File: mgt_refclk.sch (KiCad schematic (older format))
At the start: 23 parts, among them U12 5P49V6965, Y1 25MHz

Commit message: WIP: point before we change to OSH/relaxed process
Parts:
- C83, C84: value C_Small -> 100n
- R64, R65: value 10k -> 3k3
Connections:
- net I2C_SCL renamed SCL_1
- net I2C_SDA renamed SDA_1
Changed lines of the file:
@@
 $Descr A4 11693 8268
 encoding utf-8
-Sheet 18 18
+Sheet 11 18
 Title ""
 Date ""
@@
 	4250 3300 4100 3300
 Text GLabel 4050 4000 0    50   BiDi ~ 0
-I2C_SCL
+SCL_1
 Text GLabel 4050 3900 0    50   BiDi ~ 0
-I2C_SDA
+SDA_1
 Wire Wire Line
 	4050 3900 4350 3900
@@
 AR Path="/61FA7DF7/61FB7439" Ref="R64"  Part="1"
 F 0 "R64" V 4450 3750 50  0000 C CNN
-F 1 "10k" V 4300 3750 50  0000 C CNN
+F 1 "3k3" V 4300 3750 50  0000 C CNN
 F 2 "Resistor_SMD:R_0603_1608Metric" H 4200 3750 50  0001 C CNN
 F 3 "~" H 4200 3750 50  0001 C CNN
@@
 AR Path="/61FA7DF7/61FB7508" Ref="R65"  Part="1"
 F 0 "R65" V 4550 3750 50  0000 C CNN
-F 1 "10k" V 4450 3750 50  0000 C CNN
+F 1 "3k3" V 4450 3750 50  0000 C CNN
 F 2 "Resistor_SMD:R_0603_1608Metric" H 4350 3750 50  0001 C CNN
 F 3 "~" H 4350 3750 50  0001 C CNN
@@
 P 7850 3750
 F 0 "C83" V 7621 3750 50  0000 C CNN
-F 1 "C_Small" V 7712 3750 50  0000 C CNN
+F 1 "100n" V 7712 3750 50  0000 C CNN
 F 2 "Capacitor_SMD:C_0603_1608Metric" H 7850 3750 50  0001 C CNN
 F 3 "~" H 7850 3750 50  0001 C CNN
@@
 P 7850 3950
 F 0 "C84" V 8050 3950 50  0000 C CNN
-F 1 "C_Small" V 7950 3950 50  0000 C CNN
+F 1 "100n" V 7950 3950 50  0000 C CNN
 F 2 "Capacitor_SMD:C_0603_1608Metric" H 7850 3950 50  0001 C CNN
 F 3 "~" H 7850 3950 50  0001 C CNN

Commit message: further work...
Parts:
- R66: value 1k78 -> 10k
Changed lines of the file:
@@
 $Descr A4 11693 8268
 encoding utf-8
-Sheet 11 18
+Sheet 11 20
 Title ""
 Date ""
@@
 AR Path="/61FA7DF7/61FC74BB" Ref="R66"  Part="1"
 F 0 "R66" V 5750 4600 50  0000 C CNN
-F 1 "1k78" V 5950 4600 50  0000 C CNN
+F 1 "10k" V 5950 4600 50  0000 C CNN
 F 2 "Resistor_SMD:R_0603_1608Metric" H 5850 4600 50  0001 C CNN
 F 3 "~" H 5850 4600 50  0001 C CNN

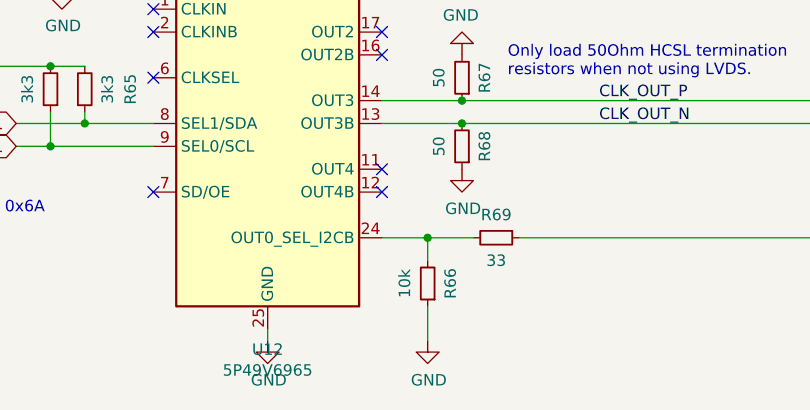
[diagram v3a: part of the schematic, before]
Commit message: mgt_refclk.sch: reduced R66 to 1k5 (see README.errata)
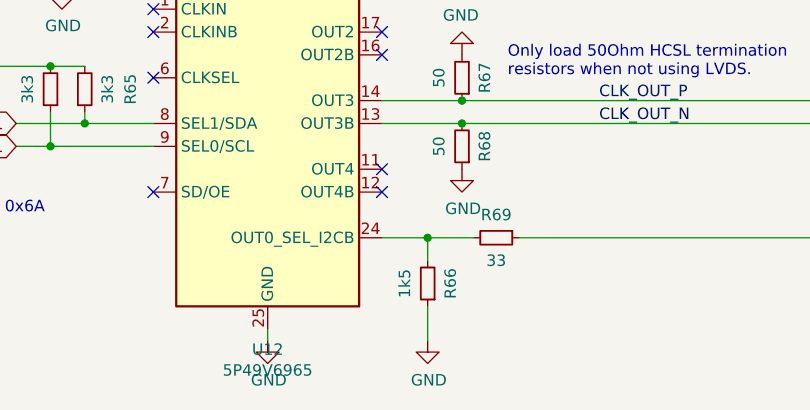
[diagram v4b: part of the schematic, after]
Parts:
- R66: value 10k -> 1k5
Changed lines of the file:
@@
 AR Path="/61FA7DF7/61FC74BB" Ref="R66"  Part="1"
 F 0 "R66" V 5750 4600 50  0000 C CNN
-F 1 "10k" V 5950 4600 50  0000 C CNN
+F 1 "1k5" V 5950 4600 50  0000 C CNN
 F 2 "Resistor_SMD:R_0603_1608Metric" H 5850 4600 50  0001 C CNN
 F 3 "~" H 5850 4600 50  0001 C CNN
